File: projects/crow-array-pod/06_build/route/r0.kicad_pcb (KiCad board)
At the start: 2 copper layers, 94.5 x 44.5 mm, 40 parts, among them J1 KF128L-3.5-8P, J2 MIC PADS (AOM-5024L), U1 OPA1678IDR

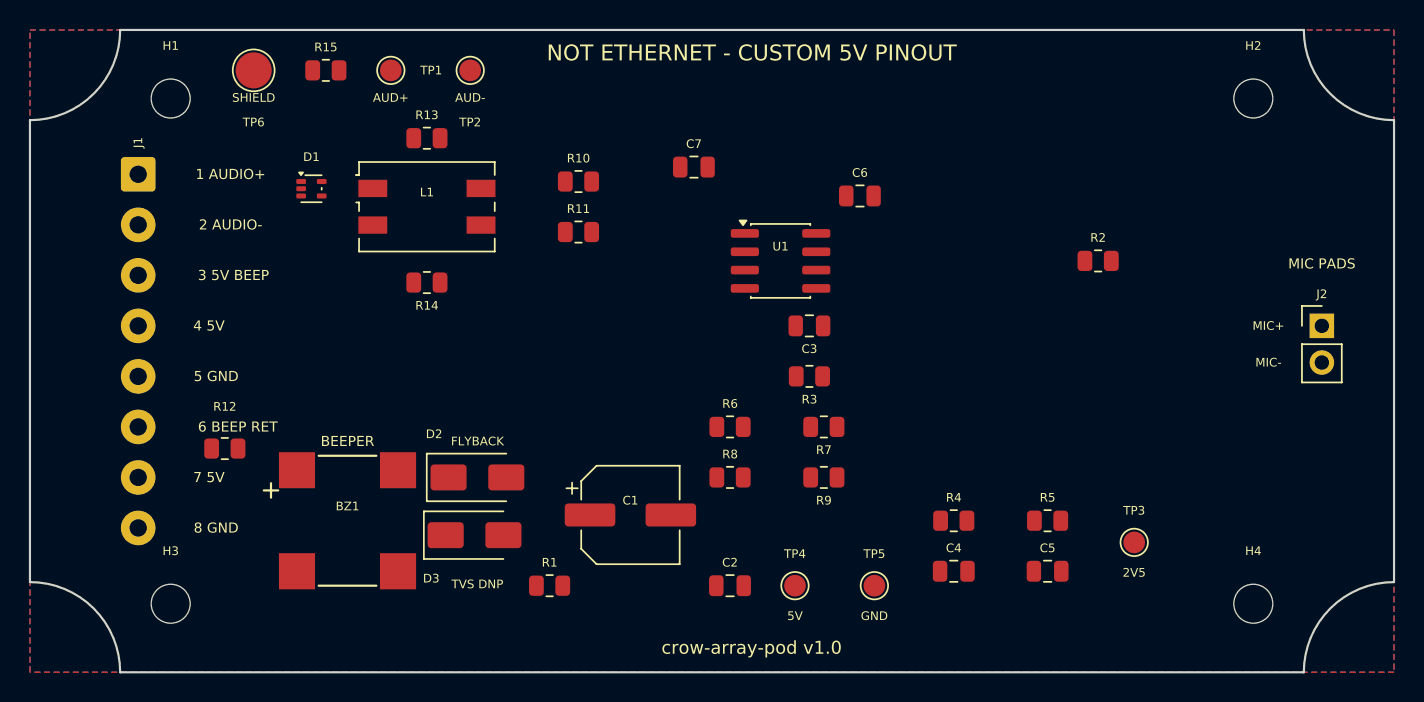
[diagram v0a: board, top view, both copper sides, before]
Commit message: crow-array-pod v1.1: RJ45 termination (A4/ADR-0004) — RJHSE-5384 jack replaces D6 screw terminal; gates ERC 0 / audit PASS / DRC 0-0-0 severity-all+parity
Net map contact-for-contact = pod v1.0 terminal map = central D28 sealed map.
Jack+plug volume inside the 1551WY lid 81x31 recess (clearance math in ADR-0004;
CONDITIONAL FIT, first-article lid-close gate). Shield -> SHIELD net (D7 provision).
Route re-run (KRT waves + GND corridor keepout + NPTH fences); stitcher gains
barrel-credit islands, strap/A* rescue, via-pad neck bridges, whisker cleanup.
S3 re-verified RJ45 pin map vs Amphenol catalogue p.4/p.6 figures (02_parts).

Co-Authored-By: Claude Fable 5 <noreply@anthropic.com>
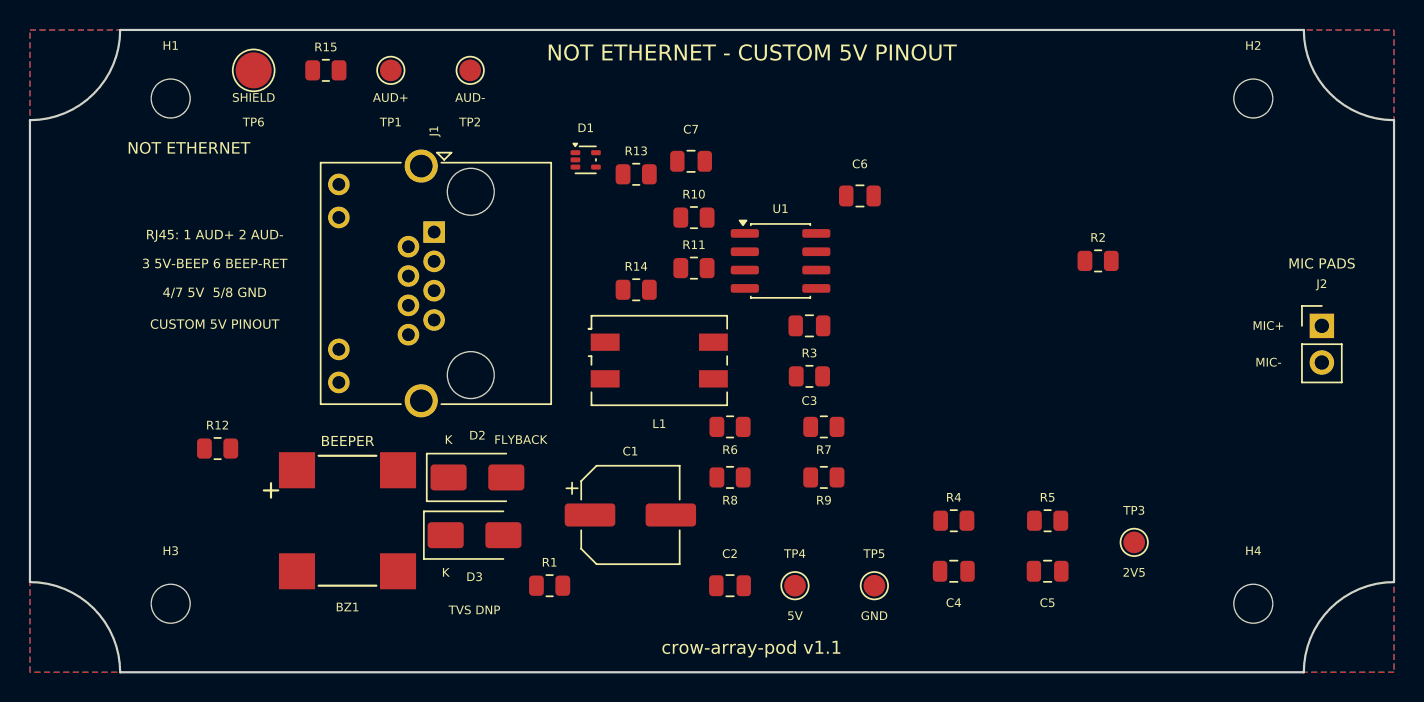
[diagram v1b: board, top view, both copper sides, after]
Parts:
- J1: value KF128L-3.5-8P -> RJHSE-5384; footprint pod:TerminalBlock_3.5-8P_NoSilk -> Connector_RJ:RJ45_Amphenol_RJHSE538X
- moved J1 20.9 mm to (78.0, 64.0)
- moved L1 19.3 mm to (93.6, 72.9)
- moved D1 19.1 mm to (88.5, 59.0)
- moved R13 14.7 mm to (92.0, 60.0)
- moved R14 14.5 mm to (92.0, 68.0)
- moved R10 8.38 mm to (96.0, 63.0)
- moved R11 8.38 mm to (96.0, 66.5)
- moved R12 0.50 mm to (63.0, 79.0)
- moved C7 0.45 mm to (95.8, 59.1)
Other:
- board text added: "3 5V-BEEP 6 BEEP-RET"
- board text added: "4/7 5V 5/8 GND"
- board text added: "CUSTOM 5V PINOUT"
- board text added: "K"
- board text added: "NOT ETHERNET"
- board text added: "RJ45: 1 AUD+ 2 AUD-"
- board text added: "crow-array-pod v1.1"
- board text removed: "1 AUDIO+"
- board text removed: "2 AUDIO-"
- board text removed: "3 5V BEEP"
- board text removed: "4 5V"
- board text removed: "5 GND"
- board text removed: "6 BEEP RET"
- board text removed: "7 5V"
- board text removed: "8 GND"
- board text removed: "crow-array-pod v1.0"

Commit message: WIP CHECKPOINT (not a gate) — pod v1.1 verification-phase files + cook-hub project skeleton; agents interrupted, preserving state before relaunch
Co-Authored-By: Claude Fable 5 <noreply@anthropic.com>
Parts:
- moved L1 18.7 mm to (93.7, 54.2)
- moved D1 9.70 mm to (88.5, 68.7)
- moved J1 7.00 mm to (78.0, 71.0), turned to 90 degrees
